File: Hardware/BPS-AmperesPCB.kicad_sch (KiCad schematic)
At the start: 8 parts, among them J1 PeripheralCAN, J2 PeripheralCAN

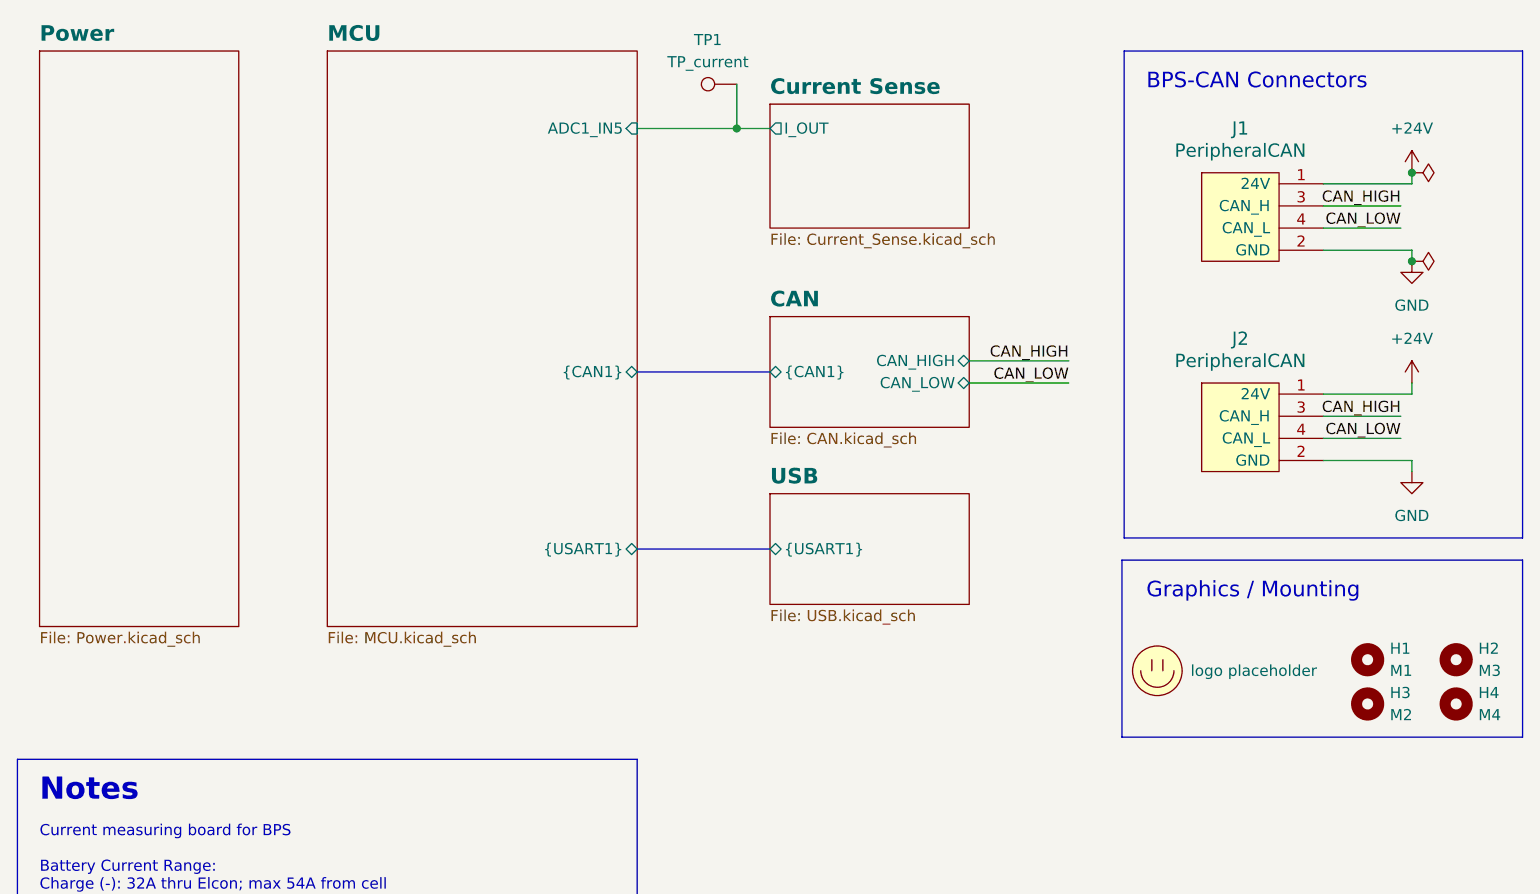
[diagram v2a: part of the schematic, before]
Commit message: changed to 2 channel op amp, stole RPP from PSOM
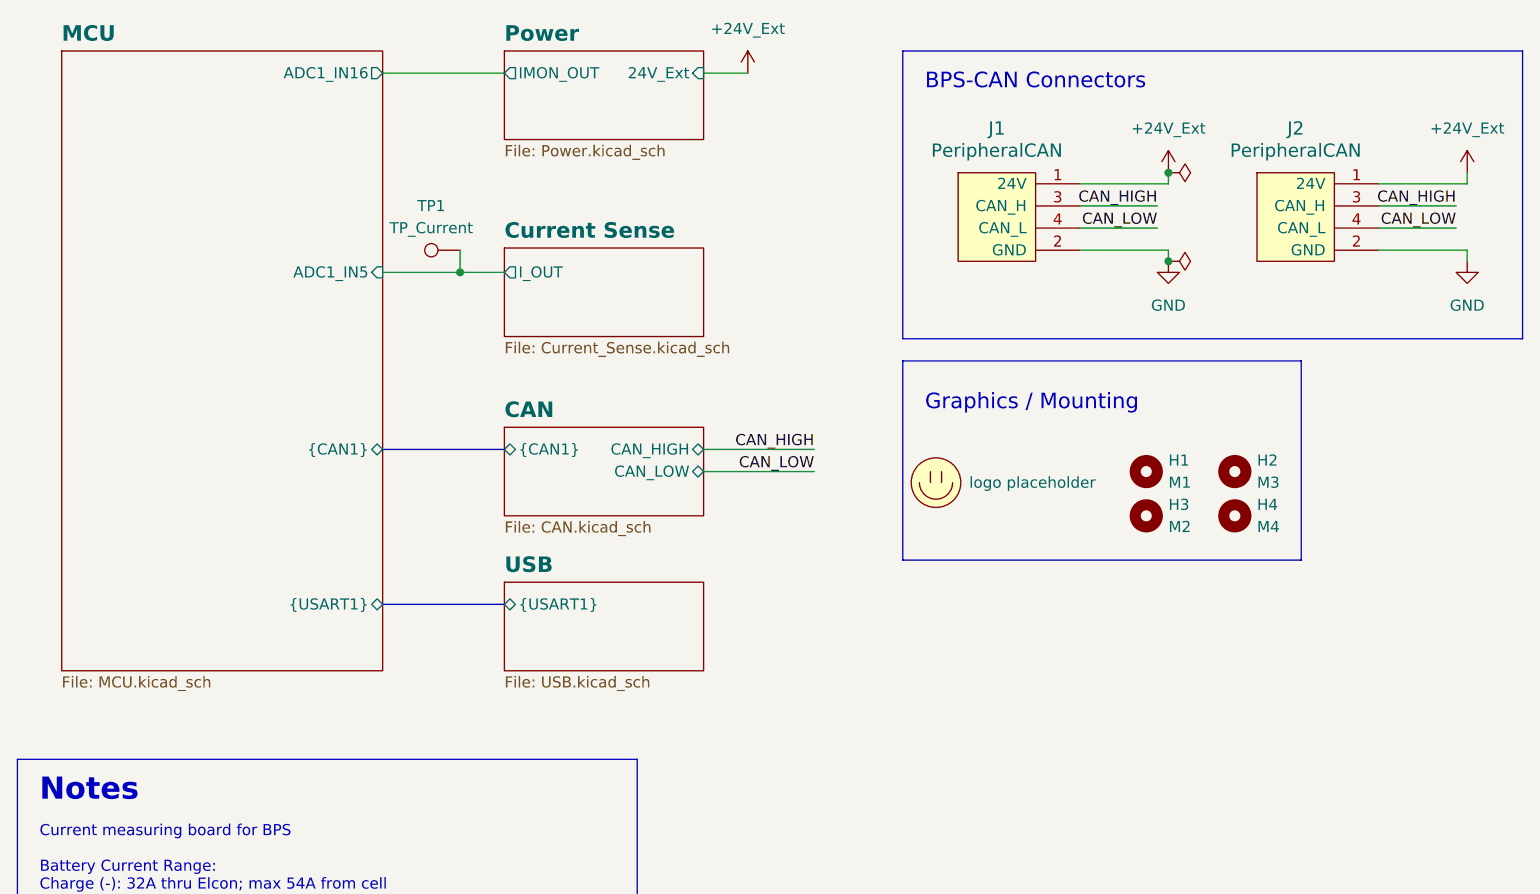
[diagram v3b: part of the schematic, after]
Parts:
- TP1: value TP_current -> TP_Current
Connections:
- net +24V renamed +24V_Ext
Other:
- sheet MCU ports: added ADC1_IN16; removed none
- sheet Power ports: added 24V_Ext, IMON_OUT; removed none
- moved on the sheet: H1, H2, H3, H4, J1, J2, TP1

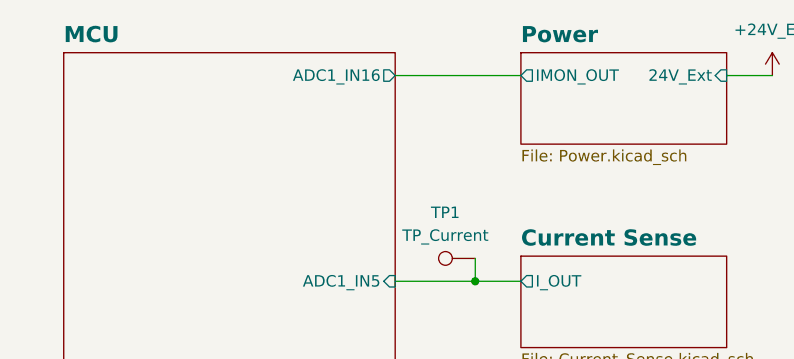
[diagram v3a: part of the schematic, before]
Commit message: added voltage reference, shunt model; addressed comments
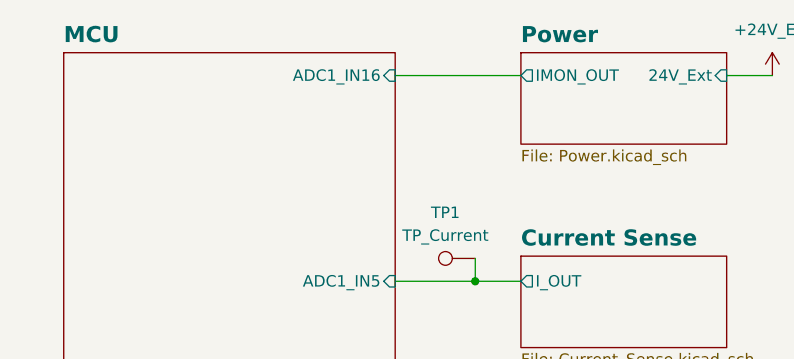
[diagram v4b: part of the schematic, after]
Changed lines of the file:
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@@
 		(on_board yes)
 		(dnp no)
-		(property "Reference" "#PWR04"
+		(property "Reference" "#PWR05"
 			(at 181.61 53.34 0)
 			(effects
@@
 			(project "BPS-AmperesPCB"
 				(path "/a452d214-ea00-440d-a445-5d6103fda43a"
-					(reference "#PWR04")
+					(reference "#PWR05")
 					(unit 1)
 				)
@@
 		(on_board yes)
 		(dnp no)
-		(property "Reference" "#PWR0121"
+		(property "Reference" "#PWR03"
 			(at 181.61 40.64 0)
 			(effects
@@
 			(project "BPS-AmperesPCB"
 				(path "/a452d214-ea00-440d-a445-5d6103fda43a"
-					(reference "#PWR0121")
+					(reference "#PWR03")
 					(unit 1)
 				)
@@
 		(on_board yes)
 		(dnp no)
-		(property "Reference" "#PWR02"
+		(property "Reference" "#PWR04"
 			(at 147.32 53.34 0)
 			(effects
@@
 			(project "BPS-AmperesPCB"
 				(path "/a452d214-ea00-440d-a445-5d6103fda43a"
-					(reference "#PWR02")
+					(reference "#PWR04")
 					(unit 1)
 				)
@@
 		(on_board yes)
 		(dnp no)
-		(property "Reference" "#PWR01"
+		(property "Reference" "#PWR02"
 			(at 147.32 40.64 0)
 			(effects
@@
 			(project "BPS-AmperesPCB"
 				(path "/a452d214-ea00-440d-a445-5d6103fda43a"
-					(reference "#PWR01")
+					(reference "#PWR02")
 					(unit 1)
 				)
@@
 		(on_board yes)
 		(dnp no)
-		(property "Reference" "#PWR03"
+		(property "Reference" "#PWR01"
 			(at 99.06 29.21 0)
 			(effects
@@
 			(project "BPS-AmperesPCB"
 				(path "/a452d214-ea00-440d-a445-5d6103fda43a"
-					(reference "#PWR03")
+					(reference "#PWR01")
 					(unit 1)
 				)
@@
 			)
 		)
-		(pin "ADC1_IN16" output
+		(pin "ADC1_IN16" input
 			(at 57.15 25.4 0)
 			(effects

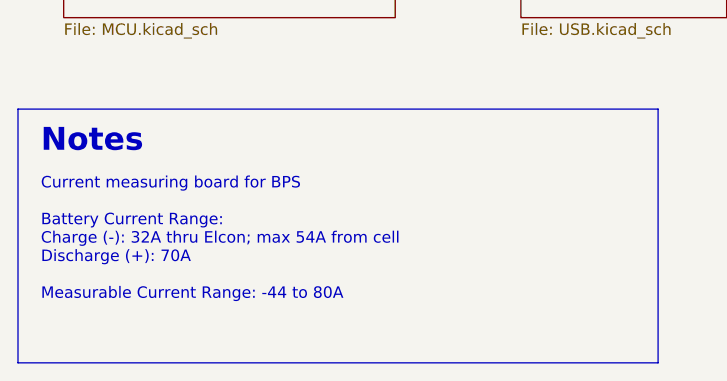
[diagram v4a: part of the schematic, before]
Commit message: added vertical usb c
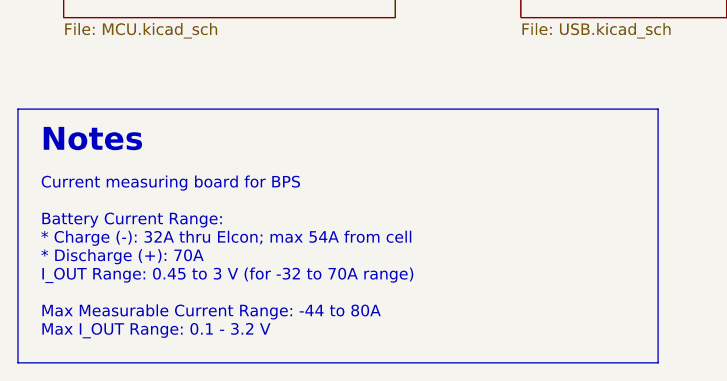
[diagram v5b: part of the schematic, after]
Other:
- note added: "Current measuring board for BPS Battery Current Range: * Charge (-): 32A thru Elcon; max 54A from cell * Discharge (+): 70A I_OUT Range: 0.45 to 3 V (for -32 to 70A range) Max Measurable Current Range: -44 to 80A Max I_OUT Range: 0.1 - 3.2 V"
- note removed: "Current measuring board for BPS Battery Current Range: Charge (-): 32A thru Elcon; max 54A from cell Discharge (+): 70A Measurable Current Range: -44 to 80A"
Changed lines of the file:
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@@
 		)
 	)
-	(text "Current measuring board for BPS\n\nBattery Current Range:\nCharge (-): 32A thru Elcon; max 54A from cell\nDischarge (+): 70A\n\nMeasurable Current Range: -44 to 80A"
+	(text "Current measuring board for BPS\n\nBattery Current Range:\n* Charge (-): 32A thru Elcon; max 54A from cell\n* Discharge (+): 70A\nI_OUT Range: 0.45 to 3 V (for -32 to 70A range)\n\nMax Measurable Current Range: -44 to 80A\nMax I_OUT Range: 0.1 - 3.2 V\n"
 		(exclude_from_sim no)
 		(at 17.78 111.76 0)
